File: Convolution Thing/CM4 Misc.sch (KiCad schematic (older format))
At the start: 6 parts

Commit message: Convolution Thing PCB design continues
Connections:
- no-connect marks 0 -> 10
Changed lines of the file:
@@
 $Descr A4 11693 8268
 encoding utf-8
-Sheet 4 4
+Sheet 4 7
 Title ""
 Date ""
@@
 Comment4 ""
 $EndDescr
-$Comp
-L CM4:Compute_Module_4_Functional U?
-U 10 1 6108B3E1
-P 4600 2400
-F 0 "U?" H 5550 2687 60  0000 C CNN
-F 1 "Compute_Module_4_Functional" H 5550 2581 60  0000 C CNN
-F 2 "" H 4800 2450 60  0001 L CNN
-F 3 "" H 4800 2250 60  0001 L CNN
-	10   4600 2400
-	1    0    0    -1
-$EndComp
 Text GLabel 6750 3850 2    50   BiDi ~ 0
 SDA
@@
 Wire Wire Line
 	4600 3300 4600 3400
-Connection ~ 4600 3400
 $Comp
 L power:GND #PWR?
@@
 Wire Wire Line
 	4350 3000 4600 3000
+Connection ~ 4600 3400
+$Comp
+L CM4:Compute_Module_4_Functional U?
+U 10 1 6108B3E1
+P 4600 2400
+F 0 "U?" H 5550 2687 60  0000 C CNN
+F 1 "Compute_Module_4_Functional" H 5550 2581 60  0000 C CNN
+F 2 "" H 4800 2450 60  0001 L CNN
+F 3 "" H 4800 2250 60  0001 L CNN
+	10   4600 2400
+	1    0    0    -1
+$EndComp
+NoConn ~ 4600 2400
+NoConn ~ 4600 2600
+NoConn ~ 4600 2800
+NoConn ~ 4600 3100
+NoConn ~ 4600 3600
+NoConn ~ 4600 3700
+NoConn ~ 4600 3800
+NoConn ~ 6500 3900
+NoConn ~ 6500 3000
+NoConn ~ 6500 2850
 $EndSCHEMATC

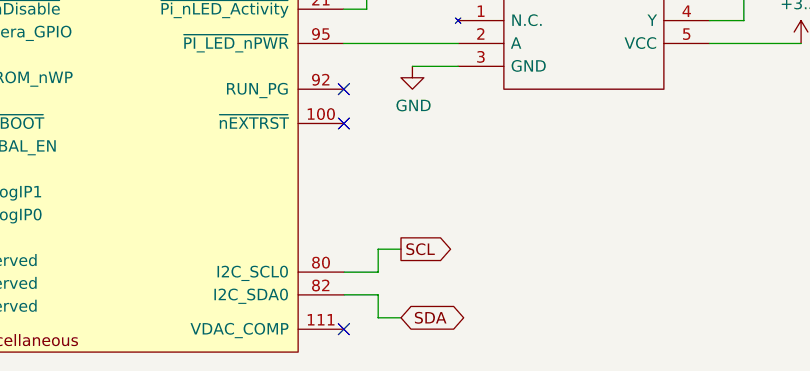
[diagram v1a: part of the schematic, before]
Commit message: New stereo codec and related changes. RIP multi-channel audio.
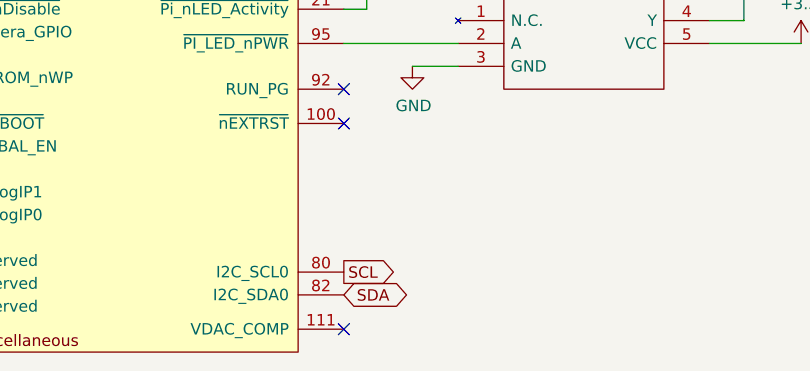
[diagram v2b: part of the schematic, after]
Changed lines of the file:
@@
 Comment4 ""
 $EndDescr
-Text GLabel 6750 3850 2    50   BiDi ~ 0
+Text GLabel 6500 3750 2    50   BiDi ~ 0
 SDA
-Text GLabel 6750 3550 2    50   Output ~ 0
+Text GLabel 6500 3650 2    50   Output ~ 0
 SCL
-Wire Wire Line
-	6500 3750 6650 3750
-Wire Wire Line
-	6650 3750 6650 3850
-Wire Wire Line
-	6650 3850 6750 3850
-Wire Wire Line
-	6500 3650 6650 3650
-Wire Wire Line
-	6650 3650 6650 3550
-Wire Wire Line
-	6650 3550 6750 3550
 $Comp
 L Device:R R?

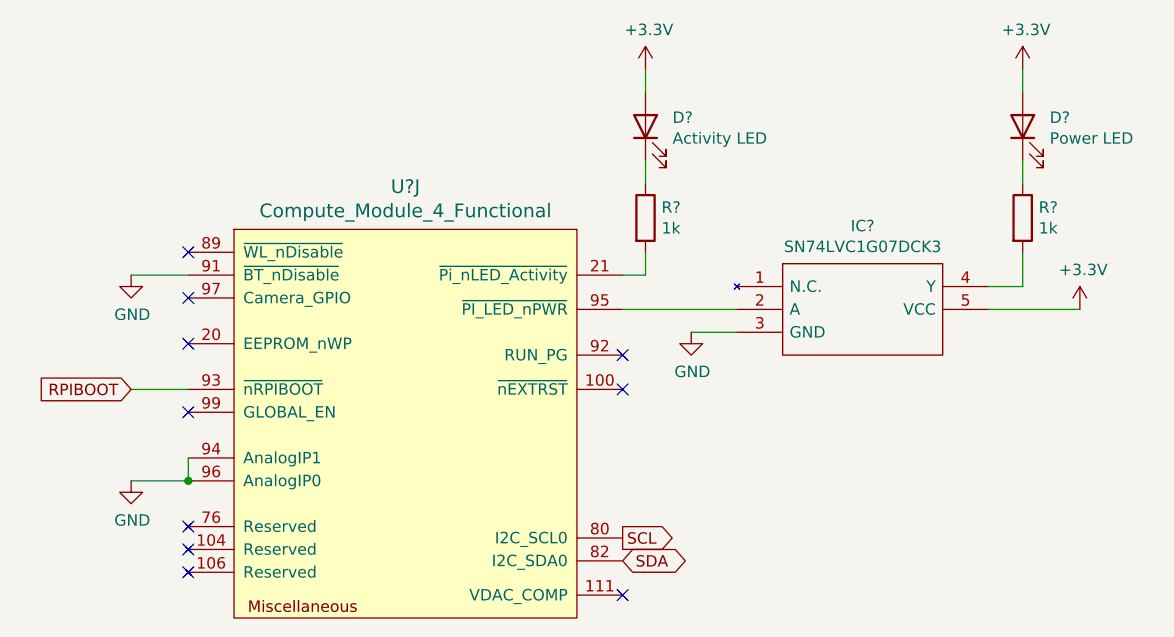
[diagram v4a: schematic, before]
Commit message: Added gate inputs and CM4 / display sockets, made CV inputs 100k, lots of smaller changes. First iteration of schematic now done.
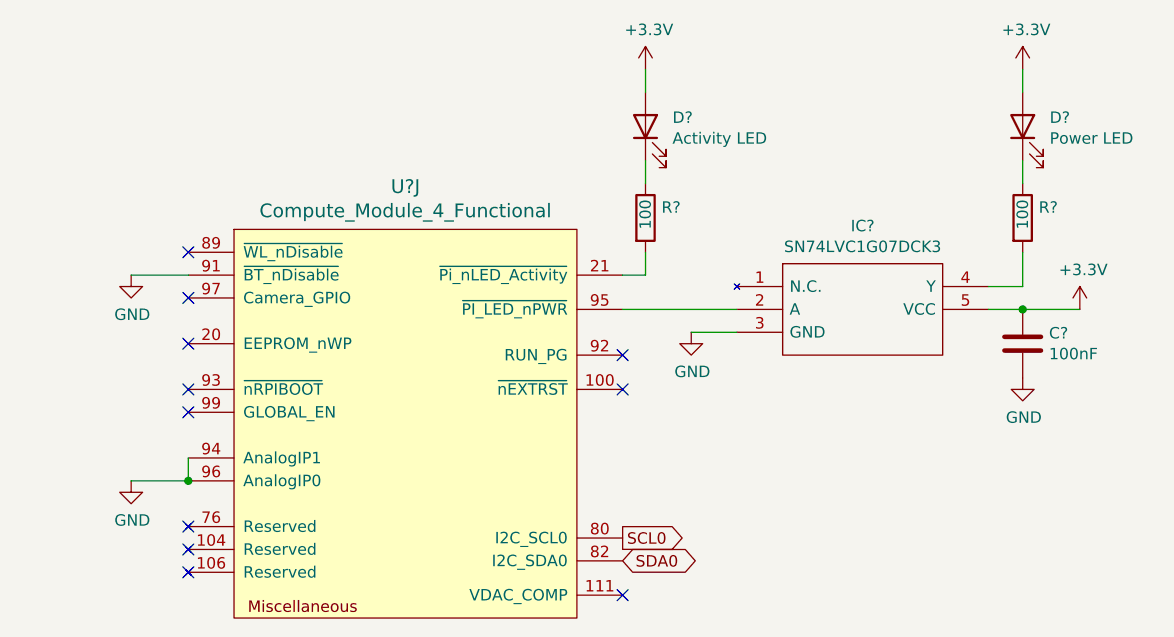
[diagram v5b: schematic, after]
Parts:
- added C?: 100nF, symbol Device:C
- R? (x2): value 1k -> 100
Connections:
- net +3V3: now also C?.1
- net GND: now also C?.2
- net RPIBOOT: no longer names the net of U?.93 (~nRPIBOOT)
- net SCL renamed SCL0
- net SDA renamed SDA0
- no-connect marks 10 -> 11
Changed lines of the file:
@@
 $Descr A4 11693 8268
 encoding utf-8
-Sheet 4 11
+Sheet 4 13
 Title ""
 Date ""
@@
 $EndDescr
 Text GLabel 6500 3750 2    50   BiDi ~ 0
-SDA
+SDA0
 Text GLabel 6500 3650 2    50   Output ~ 0
-SCL
+SCL0
 $Comp
 L Device:R R?
@@
 P 6600 2250
 F 0 "R?" H 6670 2296 50  0000 L CNN
-F 1 "1k" H 6670 2205 50  0000 L CNN
+F 1 "100" V 6600 2200 50  0000 L CNN
 F 2 "" V 6530 2250 50  0001 C CNN
 F 3 "~" H 6600 2250 50  0001 C CNN
@@
 	6800 2750 7000 2750
 Wire Wire Line
-	8500 2650 8100 2650
+	8500 2650 8250 2650
 $Comp
 L Device:LED D?
@@
 P 8250 2250
 F 0 "R?" H 8320 2296 50  0000 L CNN
-F 1 "1k" H 8320 2205 50  0000 L CNN
+F 1 "100" V 8250 2200 50  0000 L CNN
 F 2 "" V 8180 2250 50  0001 C CNN
 F 3 "~" H 8250 2250 50  0001 C CNN
@@
 Wire Wire Line
 	8250 1600 8250 1700
-Text GLabel 4350 3000 0    50   Input ~ 0
-RPIBOOT
-Wire Wire Line
-	4350 3000 4600 3000
 Connection ~ 4600 3400
 $Comp
@@
 NoConn ~ 6500 3000
 NoConn ~ 6500 2850
+NoConn ~ 4600 3000
+$Comp
+L Device:C C?
+U 1 1 612BD721
+P 8250 2800
+F 0 "C?" H 8365 2846 50  0000 L CNN
+F 1 "100nF" H 8365 2755 50  0000 L CNN
+F 2 "" H 8288 2650 50  0001 C CNN
+F 3 "~" H 8250 2800 50  0001 C CNN
+	1    8250 2800
+	1    0    0    -1
+$EndComp
+Connection ~ 8250 2650
+Wire Wire Line
+	8250 2650 8100 2650
+$Comp
+L power:GND #PWR?
+U 1 1 612BDBA0
+P 8250 2950
+F 0 "#PWR?" H 8250 2700 50  0001 C CNN
+F 1 "GND" H 8255 2777 50  0000 C CNN
+F 2 "" H 8250 2950 50  0001 C CNN
+F 3 "" H 8250 2950 50  0001 C CNN
+	1    8250 2950
+	1    0    0    -1
+$EndComp
 $EndSCHEMATC

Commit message: Fix some issues, add component references
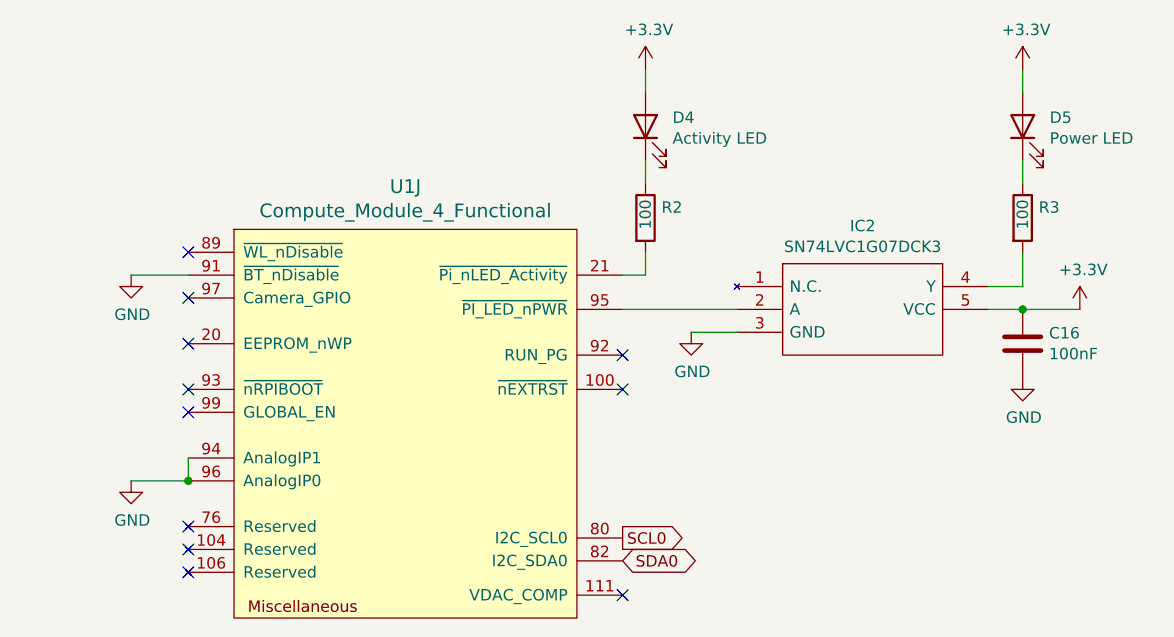
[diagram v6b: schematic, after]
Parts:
- gave numbers to parts that had none: 7
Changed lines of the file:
@@
 SCL0
 $Comp
-L Device:R R?
+L Device:R R2
 U 1 1 610937C2
 P 6600 2250
-F 0 "R?" H 6670 2296 50  0000 L CNN
+F 0 "R2" H 6670 2296 50  0000 L CNN
 F 1 "100" V 6600 2200 50  0000 L CNN
 F 2 "" V 6530 2250 50  0001 C CNN
@@
 	6600 2500 6600 2400
 $Comp
-L power:+3.3V #PWR?
+L power:+3.3V #PWR034
 U 1 1 61095024
 P 6600 1600
-F 0 "#PWR?" H 6600 1450 50  0001 C CNN
+F 0 "#PWR034" H 6600 1450 50  0001 C CNN
 F 1 "+3.3V" H 6615 1773 50  0000 C CNN
 F 2 "" H 6600 1600 50  0001 C CNN
@@
 $EndComp
 $Comp
-L Device:LED D?
+L Device:LED D4
 U 1 1 61095AE9
 P 6600 1850
-F 0 "D?" V 6639 1732 50  0000 R CNN
+F 0 "D4" V 6639 1732 50  0000 R CNN
 F 1 "Activity LED" V 6548 1732 50  0000 R CNN
 F 2 "" H 6600 1850 50  0001 C CNN
@@
 	6600 1600 6600 1700
 $Comp
-L power:GND #PWR?
+L power:GND #PWR033
 U 1 1 61097007
 P 4350 3400
-F 0 "#PWR?" H 4350 3150 50  0001 C CNN
+F 0 "#PWR033" H 4350 3150 50  0001 C CNN
 F 1 "GND" H 4355 3227 50  0000 C CNN
 F 2 "" H 4350 3400 50  0001 C CNN
@@
 	4600 3300 4600 3400
 $Comp
-L power:GND #PWR?
+L power:GND #PWR032
 U 1 1 610980BA
 P 4350 2500
-F 0 "#PWR?" H 4350 2250 50  0001 C CNN
+F 0 "#PWR032" H 4350 2250 50  0001 C CNN
 F 1 "GND" H 4355 2327 50  0000 C CNN
 F 2 "" H 4350 2500 50  0001 C CNN
@@
 	4350 2500 4600 2500
 $Comp
-L SamacSys:SN74LVC1G07DCK3 IC?
+L SamacSys:SN74LVC1G07DCK3 IC2
 U 1 1 6109BF88
 P 7000 2550
-F 0 "IC?" H 7550 2815 50  0000 C CNN
+F 0 "IC2" H 7550 2815 50  0000 C CNN
 F 1 "SN74LVC1G07DCK3" H 7550 2724 50  0000 C CNN
 F 2 "SOT65P210X110-5N" H 7950 2650 50  0001 L CNN
@@
 	7000 2650 6500 2650
 $Comp
-L power:GND #PWR?
+L power:GND #PWR035
 U 1 1 6109CCC3
 P 6800 2750
-F 0 "#PWR?" H 6800 2500 50  0001 C CNN
+F 0 "#PWR035" H 6800 2500 50  0001 C CNN
 F 1 "GND" H 6805 2577 50  0000 C CNN
 F 2 "" H 6800 2750 50  0001 C CNN
@@
 	8500 2650 8250 2650
 $Comp
-L Device:LED D?
+L Device:LED D5
 U 1 1 6109E7E2
 P 8250 1850
-F 0 "D?" V 8289 1732 50  0000 R CNN
+F 0 "D5" V 8289 1732 50  0000 R CNN
 F 1 "Power LED" V 8198 1732 50  0000 R CNN
 F 2 "" H 8250 1850 50  0001 C CNN
@@
 $EndComp
 $Comp
-L power:+3.3V #PWR?
+L power:+3.3V #PWR038
 U 1 1 6109F738
 P 8500 2650
-F 0 "#PWR?" H 8500 2500 50  0001 C CNN
+F 0 "#PWR038" H 8500 2500 50  0001 C CNN
 F 1 "+3.3V" H 8515 2823 50  0000 C CNN
 F 2 "" H 8500 2650 50  0001 C CNN
@@
 $EndComp
 $Comp
-L Device:R R?
+L Device:R R3
 U 1 1 6109FB2A
 P 8250 2250
-F 0 "R?" H 8320 2296 50  0000 L CNN
+F 0 "R3" H 8320 2296 50  0000 L CNN
 F 1 "100" V 8250 2200 50  0000 L CNN
 F 2 "" V 8180 2250 50  0001 C CNN
@@
 	8250 2550 8100 2550
 $Comp
-L power:+3.3V #PWR?
+L power:+3.3V #PWR036
 U 1 1 610A06BC
 P 8250 1600
-F 0 "#PWR?" H 8250 1450 50  0001 C CNN
+F 0 "#PWR036" H 8250 1450 50  0001 C CNN
 F 1 "+3.3V" H 8265 1773 50  0000 C CNN
 F 2 "" H 8250 1600 50  0001 C CNN
@@
 Connection ~ 4600 3400
 $Comp
-L CM4:Compute_Module_4_Functional U?
+L CM4:Compute_Module_4_Functional U1
 U 10 1 6108B3E1
 P 4600 2400
-F 0 "U?" H 5550 2687 60  0000 C CNN
+F 0 "U1" H 5550 2687 60  0000 C CNN
 F 1 "Compute_Module_4_Functional" H 5550 2581 60  0000 C CNN
 F 2 "" H 4800 2450 60  0001 L CNN
@@
 NoConn ~ 4600 3000
 $Comp
-L Device:C C?
+L Device:C C16
 U 1 1 612BD721
 P 8250 2800
-F 0 "C?" H 8365 2846 50  0000 L CNN
+F 0 "C16" H 8365 2846 50  0000 L CNN
 F 1 "100nF" H 8365 2755 50  0000 L CNN
 F 2 "" H 8288 2650 50  0001 C CNN
@@
 	8250 2650 8100 2650
 $Comp
-L power:GND #PWR?
+L power:GND #PWR037
 U 1 1 612BDBA0
 P 8250 2950
-F 0 "#PWR?" H 8250 2700 50  0001 C CNN
+F 0 "#PWR037" H 8250 2700 50  0001 C CNN
 F 1 "GND" H 8255 2777 50  0000 C CNN
 F 2 "" H 8250 2950 50  0001 C CNN

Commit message: Started footprint assignment
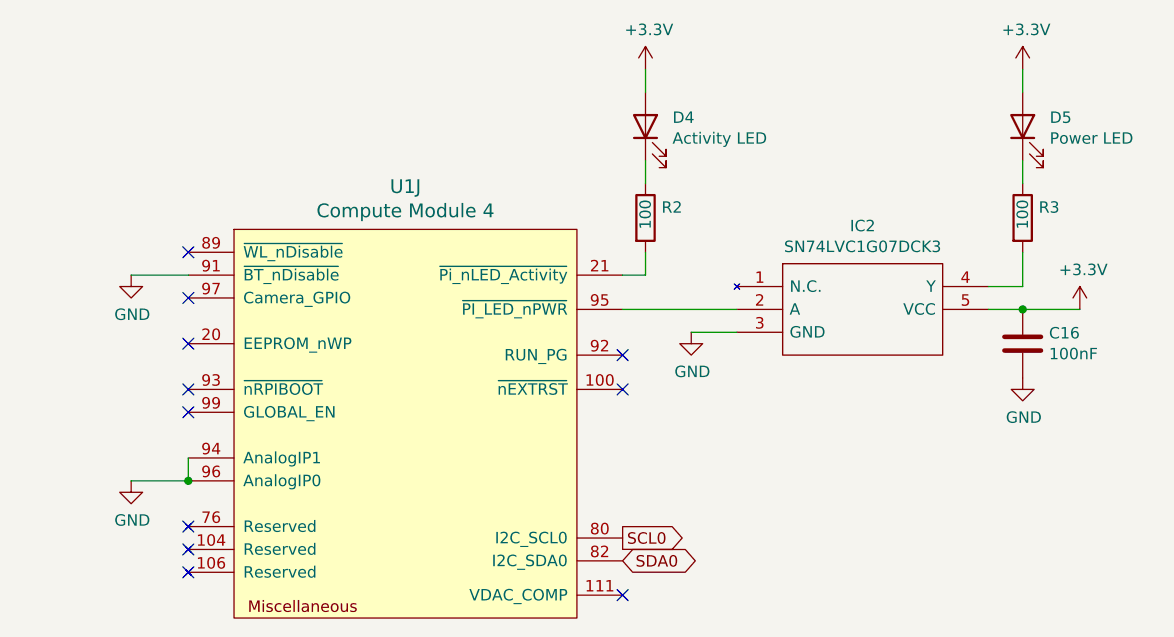
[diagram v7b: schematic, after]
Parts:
- IC2: footprint SOT65P210X110-5N -> SamacSys:SOT65P210X110-5N
- U1: value Compute_Module_4_Functional -> Compute Module 4; footprint (none) -> CM4:Raspberry-Pi-4-Compute-Module
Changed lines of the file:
@@
 F 0 "IC2" H 7550 2815 50  0000 C CNN
 F 1 "SN74LVC1G07DCK3" H 7550 2724 50  0000 C CNN
-F 2 "SOT65P210X110-5N" H 7950 2650 50  0001 L CNN
+F 2 "SamacSys:SOT65P210X110-5N" H 7950 2650 50  0001 L CNN
 F 3 "http://www.ti.com/general/docs/suppproductinfo.tsp?distId=10&gotoUrl=http%3A%2F%2Fwww.ti.com%2Flit%2Fgpn%2FSN74LVC1G07" H 7950 2550 50  0001 L CNN
 F 4 "Buffers & Line Drivers Single Buffer/Driver With Open-Drain Output 5-SC70 -40 to 125" H 7950 2450 50  0001 L CNN "Description"
@@
 P 4600 2400
 F 0 "U1" H 5550 2687 60  0000 C CNN
-F 1 "Compute_Module_4_Functional" H 5550 2581 60  0000 C CNN
-F 2 "" H 4800 2450 60  0001 L CNN
+F 1 "Compute Module 4" H 5550 2581 60  0000 C CNN
+F 2 "CM4:Raspberry-Pi-4-Compute-Module" H 4800 2450 60  0001 L CNN
 F 3 "" H 4800 2250 60  0001 L CNN
 	10   4600 2400

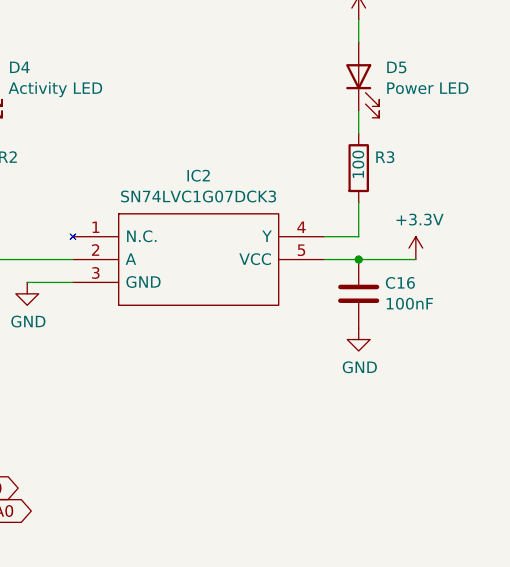
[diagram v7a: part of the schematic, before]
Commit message: Assign all footprints
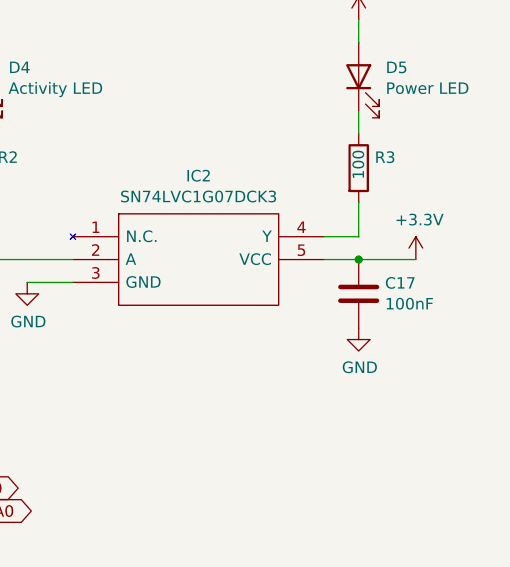
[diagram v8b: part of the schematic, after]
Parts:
- C17: renamed from C16; footprint (none) -> Capacitor_SMD:C_0805_2012Metric
- D4, D5: footprint (none) -> LED_SMD:LED_0805_2012Metric
- R2, R3: footprint (none) -> Resistor_SMD:R_0805_2012Metric
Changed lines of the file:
@@
 F 0 "R2" H 6670 2296 50  0000 L CNN
 F 1 "100" V 6600 2200 50  0000 L CNN
-F 2 "" V 6530 2250 50  0001 C CNN
+F 2 "Resistor_SMD:R_0805_2012Metric" V 6530 2250 50  0001 C CNN
 F 3 "~" H 6600 2250 50  0001 C CNN
 	1    6600 2250
@@
 	6600 2500 6600 2400
 $Comp
-L power:+3.3V #PWR034
+L power:+3.3V #PWR035
 U 1 1 61095024
 P 6600 1600
-F 0 "#PWR034" H 6600 1450 50  0001 C CNN
+F 0 "#PWR035" H 6600 1450 50  0001 C CNN
 F 1 "+3.3V" H 6615 1773 50  0000 C CNN
 F 2 "" H 6600 1600 50  0001 C CNN
@@
 F 0 "D4" V 6639 1732 50  0000 R CNN
 F 1 "Activity LED" V 6548 1732 50  0000 R CNN
-F 2 "" H 6600 1850 50  0001 C CNN
+F 2 "LED_SMD:LED_0805_2012Metric" H 6600 1850 50  0001 C CNN
 F 3 "~" H 6600 1850 50  0001 C CNN
 	1    6600 1850
@@
 	6600 1600 6600 1700
 $Comp
-L power:GND #PWR033
+L power:GND #PWR034
 U 1 1 61097007
 P 4350 3400
-F 0 "#PWR033" H 4350 3150 50  0001 C CNN
+F 0 "#PWR034" H 4350 3150 50  0001 C CNN
 F 1 "GND" H 4355 3227 50  0000 C CNN
 F 2 "" H 4350 3400 50  0001 C CNN
@@
 	4600 3300 4600 3400
 $Comp
-L power:GND #PWR032
+L power:GND #PWR033
 U 1 1 610980BA
 P 4350 2500
-F 0 "#PWR032" H 4350 2250 50  0001 C CNN
+F 0 "#PWR033" H 4350 2250 50  0001 C CNN
 F 1 "GND" H 4355 2327 50  0000 C CNN
 F 2 "" H 4350 2500 50  0001 C CNN
@@
 	7000 2650 6500 2650
 $Comp
-L power:GND #PWR035
+L power:GND #PWR036
 U 1 1 6109CCC3
 P 6800 2750
-F 0 "#PWR035" H 6800 2500 50  0001 C CNN
+F 0 "#PWR036" H 6800 2500 50  0001 C CNN
 F 1 "GND" H 6805 2577 50  0000 C CNN
 F 2 "" H 6800 2750 50  0001 C CNN
@@
 F 0 "D5" V 8289 1732 50  0000 R CNN
 F 1 "Power LED" V 8198 1732 50  0000 R CNN
-F 2 "" H 8250 1850 50  0001 C CNN
+F 2 "LED_SMD:LED_0805_2012Metric" H 8250 1850 50  0001 C CNN
 F 3 "~" H 8250 1850 50  0001 C CNN
 	1    8250 1850
@@
 $EndComp
 $Comp
-L power:+3.3V #PWR038
+L power:+3.3V #PWR039
 U 1 1 6109F738
 P 8500 2650
-F 0 "#PWR038" H 8500 2500 50  0001 C CNN
+F 0 "#PWR039" H 8500 2500 50  0001 C CNN
 F 1 "+3.3V" H 8515 2823 50  0000 C CNN
 F 2 "" H 8500 2650 50  0001 C CNN
@@
 F 0 "R3" H 8320 2296 50  0000 L CNN
 F 1 "100" V 8250 2200 50  0000 L CNN
-F 2 "" V 8180 2250 50  0001 C CNN
+F 2 "Resistor_SMD:R_0805_2012Metric" V 8180 2250 50  0001 C CNN
 F 3 "~" H 8250 2250 50  0001 C CNN
 	1    8250 2250
@@
 	8250 2550 8100 2550
 $Comp
-L power:+3.3V #PWR036
+L power:+3.3V #PWR037
 U 1 1 610A06BC
 P 8250 1600
-F 0 "#PWR036" H 8250 1450 50  0001 C CNN
+F 0 "#PWR037" H 8250 1450 50  0001 C CNN
 F 1 "+3.3V" H 8265 1773 50  0000 C CNN
 F 2 "" H 8250 1600 50  0001 C CNN
@@
 NoConn ~ 4600 3000
 $Comp
-L Device:C C16
+L Device:C C17
 U 1 1 612BD721
 P 8250 2800
-F 0 "C16" H 8365 2846 50  0000 L CNN
+F 0 "C17" H 8365 2846 50  0000 L CNN
 F 1 "100nF" H 8365 2755 50  0000 L CNN
-F 2 "" H 8288 2650 50  0001 C CNN
+F 2 "Capacitor_SMD:C_0805_2012Metric" H 8288 2650 50  0001 C CNN
 F 3 "~" H 8250 2800 50  0001 C CNN
 	1    8250 2800
@@
 	8250 2650 8100 2650
 $Comp
-L power:GND #PWR037
+L power:GND #PWR038
 U 1 1 612BDBA0
 P 8250 2950
-F 0 "#PWR037" H 8250 2700 50  0001 C CNN
+F 0 "#PWR038" H 8250 2700 50  0001 C CNN
 F 1 "GND" H 8255 2777 50  0000 C CNN
 F 2 "" H 8250 2950 50  0001 C CNN
